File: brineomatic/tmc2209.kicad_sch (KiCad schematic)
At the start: 17 parts, among them J21 Conn_01x04, U9 TMC2209-LA

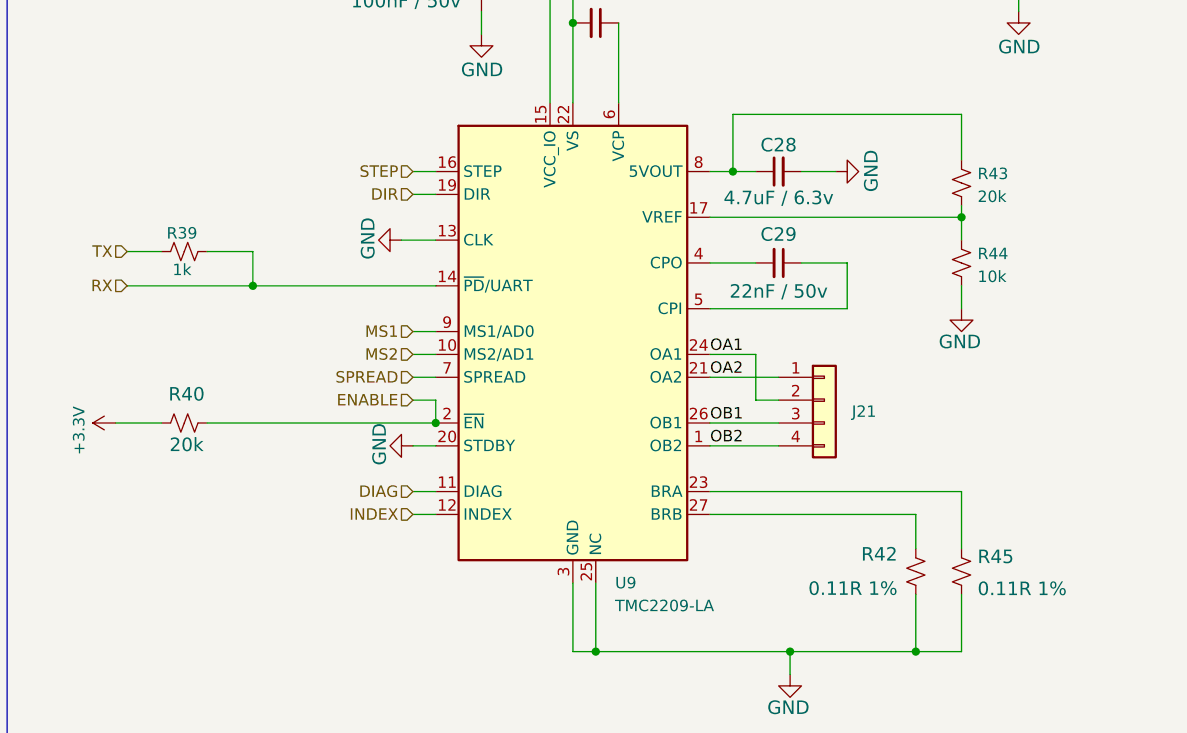
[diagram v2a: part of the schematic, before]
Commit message: switch to rt7272b for 24v -> 5v regulator
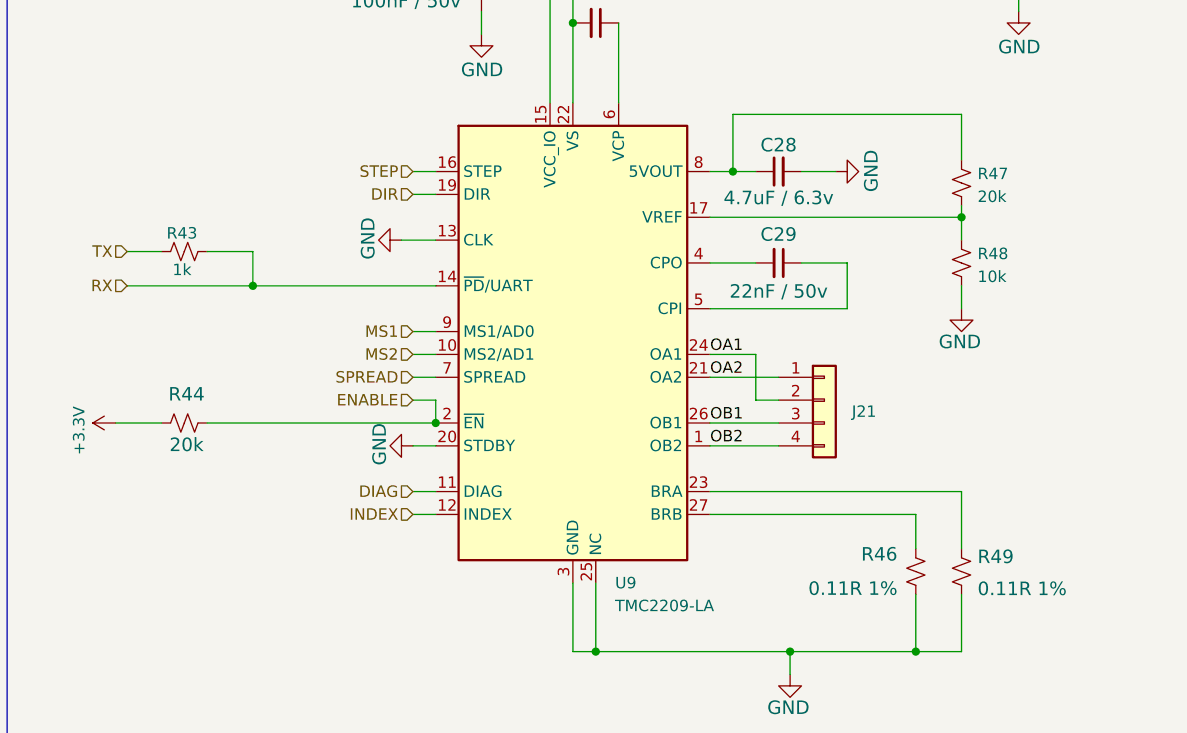
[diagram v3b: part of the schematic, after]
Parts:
- renumbered R39 to R43, R40 to R44, R42 to R46, R43 to R47, R44 to R48, R45 to R49
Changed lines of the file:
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@@
 		(on_board yes)
 		(dnp no)
-		(property "Reference" "R40"
+		(property "Reference" "R44"
 			(at 38.354 108.966 90)
 			(effects
@@
 			(project "brineomatic"
 				(path "/96477ae2-ef08-48f3-8dd4-fe4478541f68/0f01c39f-0c25-414e-9ed3-1ba09e2af0c5"
-					(reference "R40")
+					(reference "R44")
 					(unit 1)
 				)
@@
 		(on_board yes)
 		(dnp no)
-		(property "Reference" "R45"
+		(property "Reference" "R49"
 			(at 126.238 128.778 0)
 			(effects
@@
 			(project "brineomatic"
 				(path "/96477ae2-ef08-48f3-8dd4-fe4478541f68/0f01c39f-0c25-414e-9ed3-1ba09e2af0c5"
-					(reference "R45")
+					(reference "R49")
 					(unit 1)
 				)
@@
 		(on_board yes)
 		(dnp no)
-		(property "Reference" "R39"
+		(property "Reference" "R43"
 			(at 37.846 91.948 90)
 			(effects
@@
 			(project "brineomatic"
 				(path "/96477ae2-ef08-48f3-8dd4-fe4478541f68/0f01c39f-0c25-414e-9ed3-1ba09e2af0c5"
-					(reference "R39")
+					(reference "R43")
 					(unit 1)
 				)
@@
 		(on_board yes)
 		(dnp no)
-		(property "Reference" "#PWR063"
+		(property "Reference" "#PWR061"
 			(at 74.93 63.5 0)
 			(effects
@@
 			(project "brineomatic"
 				(path "/96477ae2-ef08-48f3-8dd4-fe4478541f68/0f01c39f-0c25-414e-9ed3-1ba09e2af0c5"
-					(reference "#PWR063")
+					(reference "#PWR061")
 					(unit 1)
 				)
@@
 		(on_board yes)
 		(dnp no)
-		(property "Reference" "R42"
+		(property "Reference" "R46"
 			(at 117.348 126.746 0)
 			(effects
@@
 			(project "brineomatic"
 				(path "/96477ae2-ef08-48f3-8dd4-fe4478541f68/0f01c39f-0c25-414e-9ed3-1ba09e2af0c5"
-					(reference "R42")
+					(reference "R46")
 					(unit 1)
 				)
@@
 		(on_board yes)
 		(dnp no)
-		(property "Reference" "#PWR062"
+		(property "Reference" "#PWR060"
 			(at 34.29 113.03 0)
 			(effects
@@
 			(project "brineomatic"
 				(path "/96477ae2-ef08-48f3-8dd4-fe4478541f68/0f01c39f-0c25-414e-9ed3-1ba09e2af0c5"
-					(reference "#PWR062")
+					(reference "#PWR060")
 					(unit 1)
 				)
@@
 		(on_board yes)
 		(dnp no)
-		(property "Reference" "R43"
+		(property "Reference" "R47"
 			(at 126.238 85.344 0)
 			(effects
@@
 			(project "brineomatic"
 				(path "/96477ae2-ef08-48f3-8dd4-fe4478541f68/0f01c39f-0c25-414e-9ed3-1ba09e2af0c5"
-					(reference "R43")
+					(reference "R47")
 					(unit 1)
 				)
@@
 		(dnp no)
 		(fields_autoplaced yes)
-		(property "Reference" "#PWR064"
+		(property "Reference" "#PWR062"
 			(at 81.28 52.07 0)
 			(effects
@@
 			(project ""
 				(path "/96477ae2-ef08-48f3-8dd4-fe4478541f68/0f01c39f-0c25-414e-9ed3-1ba09e2af0c5"
-					(reference "#PWR064")
+					(reference "#PWR062")
 					(unit 1)
 				)
@@
 		(on_board yes)
 		(dnp no)
-		(property "Reference" "R44"
+		(property "Reference" "R48"
 			(at 126.238 94.234 0)
 			(effects
@@
 			(project "brineomatic"
 				(path "/96477ae2-ef08-48f3-8dd4-fe4478541f68/0f01c39f-0c25-414e-9ed3-1ba09e2af0c5"
-					(reference "R44")
-					(unit 1)
-				)
+					(reference "R48")
+					(unit 1)
+				)

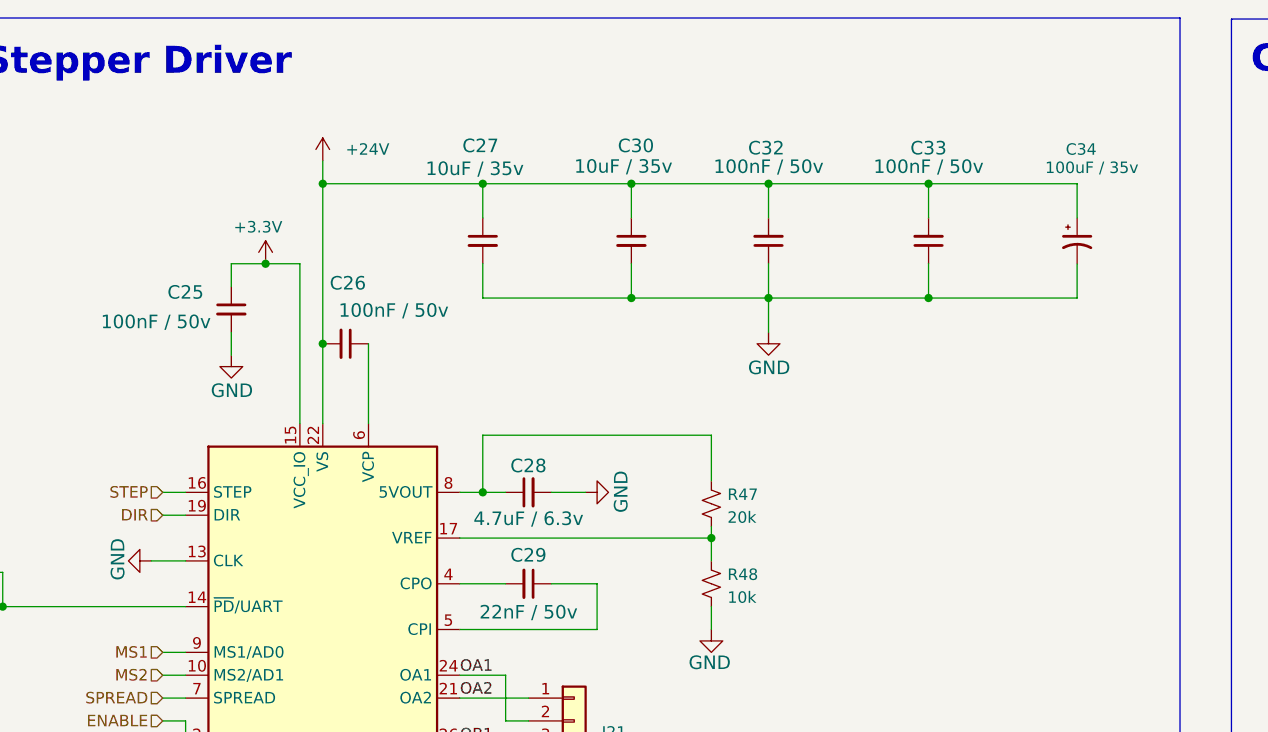
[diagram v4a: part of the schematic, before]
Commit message: added bulk cap to 5v rail and tidied silkscreen
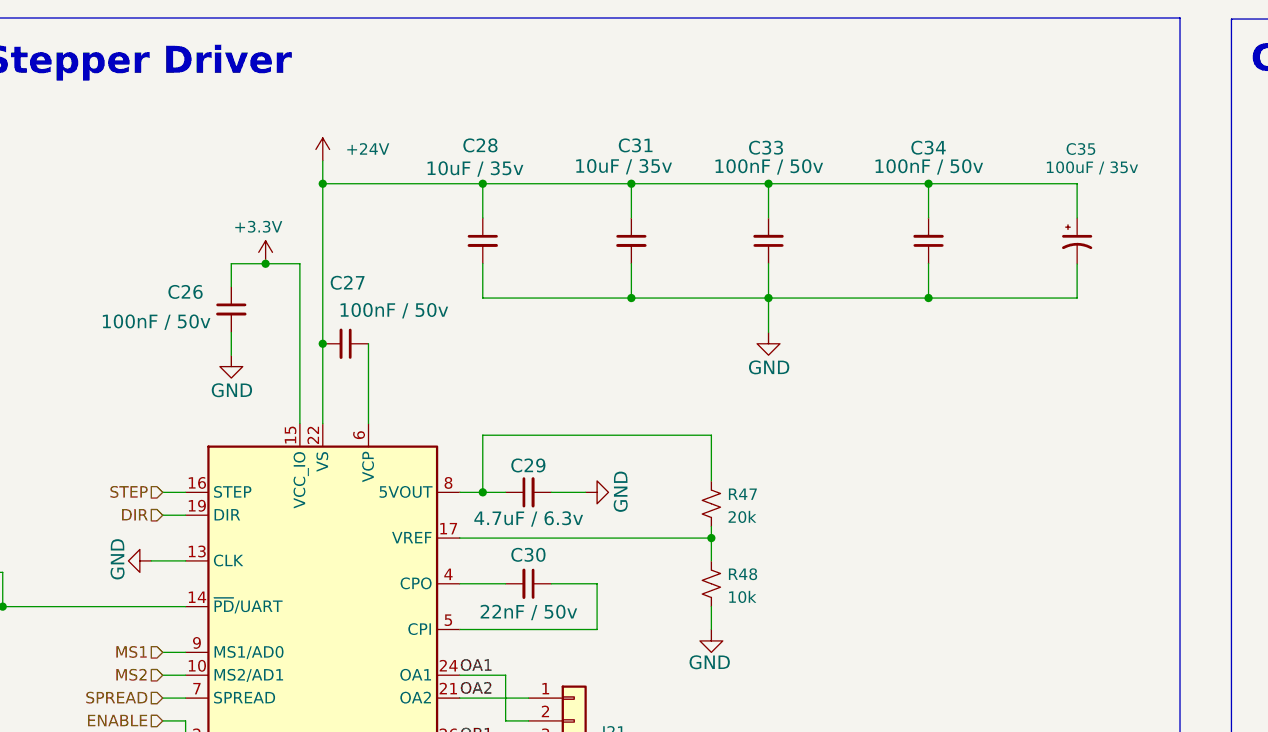
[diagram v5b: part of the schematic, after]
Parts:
- renumbered C25 to C26, C26 to C27, C27 to C28, C28 to C29, C29 to C30, C30 to C31, C32 to C33, C33 to C34, C34 to C35
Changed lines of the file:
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@@
 		(on_board yes)
 		(dnp no)
-		(property "Reference" "C30"
+		(property "Reference" "C31"
 			(at 118.11 45.72 0)
 			(effects
@@
 			(project "brineomatic"
 				(path "/96477ae2-ef08-48f3-8dd4-fe4478541f68/0f01c39f-0c25-414e-9ed3-1ba09e2af0c5"
-					(reference "C30")
+					(reference "C31")
 					(unit 1)
 				)
@@
 		(on_board yes)
 		(dnp no)
-		(property "Reference" "C33"
+		(property "Reference" "C34"
 			(at 148.59 45.974 0)
 			(effects
@@
 			(project "brineomatic"
 				(path "/96477ae2-ef08-48f3-8dd4-fe4478541f68/0f01c39f-0c25-414e-9ed3-1ba09e2af0c5"
-					(reference "C33")
+					(reference "C34")
 					(unit 1)
 				)
@@
 		(on_board yes)
 		(dnp no)
-		(property "Reference" "C26"
+		(property "Reference" "C27"
 			(at 84.074 62.738 90)
 			(effects
@@
 			(project "brineomatic"
 				(path "/96477ae2-ef08-48f3-8dd4-fe4478541f68/0f01c39f-0c25-414e-9ed3-1ba09e2af0c5"
-					(reference "C26")
+					(reference "C27")
 					(unit 1)
 				)
@@
 		(on_board yes)
 		(dnp no)
-		(property "Reference" "C34"
+		(property "Reference" "C35"
 			(at 163.83 46.99 0)
 			(effects
@@
 			(project ""
 				(path "/96477ae2-ef08-48f3-8dd4-fe4478541f68/0f01c39f-0c25-414e-9ed3-1ba09e2af0c5"
-					(reference "C34")
+					(reference "C35")
 					(unit 1)
 				)
@@
 		(on_board yes)
 		(dnp no)
-		(property "Reference" "C27"
+		(property "Reference" "C28"
 			(at 100.838 45.72 0)
 			(effects
@@
 			(project "brineomatic"
 				(path "/96477ae2-ef08-48f3-8dd4-fe4478541f68/0f01c39f-0c25-414e-9ed3-1ba09e2af0c5"
-					(reference "C27")
+					(reference "C28")
 					(unit 1)
 				)
@@
 		(on_board yes)
 		(dnp no)
-		(property "Reference" "C25"
+		(property "Reference" "C26"
 			(at 66.04 63.754 0)
 			(effects
@@
 			(project "brineomatic"
 				(path "/96477ae2-ef08-48f3-8dd4-fe4478541f68/0f01c39f-0c25-414e-9ed3-1ba09e2af0c5"
-					(reference "C25")
+					(reference "C26")
 					(unit 1)
 				)
@@
 		(on_board yes)
 		(dnp no)
-		(property "Reference" "C29"
+		(property "Reference" "C30"
 			(at 104.14 92.964 90)
 			(effects
@@
 			(project "brineomatic"
 				(path "/96477ae2-ef08-48f3-8dd4-fe4478541f68/0f01c39f-0c25-414e-9ed3-1ba09e2af0c5"
-					(reference "C29")
+					(reference "C30")
 					(unit 1)
 				)
@@
 		(on_board yes)
 		(dnp no)
-		(property "Reference" "C28"
+		(property "Reference" "C29"
 			(at 104.14 81.28 90)
 			(effects
@@
 			(project "brineomatic"
 				(path "/96477ae2-ef08-48f3-8dd4-fe4478541f68/0f01c39f-0c25-414e-9ed3-1ba09e2af0c5"
-					(reference "C28")
+					(reference "C29")
 					(unit 1)
 				)
@@
 		(on_board yes)
 		(dnp no)
-		(property "Reference" "C32"
+		(property "Reference" "C33"
 			(at 130.556 45.974 0)
 			(effects
@@
 			(project "brineomatic"
 				(path "/96477ae2-ef08-48f3-8dd4-fe4478541f68/0f01c39f-0c25-414e-9ed3-1ba09e2af0c5"
-					(reference "C32")
-					(unit 1)
-				)
+					(reference "C33")
+					(unit 1)
+				)

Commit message: tested and update bom + placement
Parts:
- C26, C27: value 100nF / 50v -> 100nF; LCSC (none) -> C14663
- C29: value 4.7uF / 6.3v -> 4.7uF; LCSC (none) -> C19666
- C30: LCSC C21122 -> (none)
- C33, C34: value 100nF / 50v -> 100nF; footprint Capacitor_SMD:C_0402_1005Metric -> Capacitor_SMD:C_0603_1608Metric; LCSC (none) -> C14663
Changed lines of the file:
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@@
 			)
 		)
-		(property "Value" "100nF / 50v"
+		(property "Value" "100nF"
 			(at 148.59 49.784 0)
 			(effects
@@
 			)
 		)
-		(property "Footprint" "Capacitor_SMD:C_0402_1005Metric"
+		(property "Footprint" "Capacitor_SMD:C_0603_1608Metric"
 			(at 148.59 57.15 0)
 			(effects
@@
 			)
 		)
-		(property "LCSC" ""
+		(property "LCSC" "C14663"
 			(at 148.59 57.15 0)
 			(effects
@@
 			)
 		)
-		(property "Value" "100nF / 50v"
+		(property "Value" "100nF"
 			(at 89.154 64.008 90)
 			(effects
@@
 			)
 		)
-		(property "LCSC" ""
+		(property "LCSC" "C14663"
 			(at 83.82 68.58 90)
 			(effects
@@
 			)
 		)
-		(property "Value" "100nF / 50v"
+		(property "Value" "100nF"
 			(at 62.738 65.278 0)
 			(effects
@@
 			)
 		)
-		(property "LCSC" ""
+		(property "LCSC" "C14663"
 			(at 71.12 64.77 0)
 			(effects
@@
 			)
 		)
-		(property "LCSC" "C21122"
+		(property "LCSC" ""
 			(at 104.14 95.25 90)
 			(effects
@@
 			)
 		)
-		(property "Value" "4.7uF / 6.3v"
+		(property "Value" "4.7uF"
 			(at 104.14 88.9 90)
 			(effects
@@
 			)
 		)
-		(property "LCSC" ""
+		(property "LCSC" "C19666"
 			(at 104.14 85.09 90)
 			(effects
@@
 			)
 		)
-		(property "Value" "100nF / 50v"
+		(property "Value" "100nF"
 			(at 130.81 49.784 0)
 			(effects
@@
 			)
 		)
-		(property "Footprint" "Capacitor_SMD:C_0402_1005Metric"
+		(property "Footprint" "Capacitor_SMD:C_0603_1608Metric"
 			(at 130.81 57.15 0)
 			(effects
@@
 			)
 		)
-		(property "LCSC" ""
+		(property "LCSC" "C14663"
 			(at 130.81 57.15 0)
 			(effects

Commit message: updated resistor p/ns in bom
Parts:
- R43: LCSC (none) -> C21190
- R44, R47: LCSC (none) -> C4184
- R48: LCSC (none) -> C25804
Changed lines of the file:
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@@
+			)
+		)
+		(property "LCSC" " C4184"
+			(at 38.1 113.03 90)
+			(effects
+				(font
+					(size 1.27 1.27)
+				)
+				(hide yes)
 			)
 		)
@@
 		(property "Description" "Resistor, small US symbol"
 			(at 38.1 93.98 0)
+			(effects
+				(font
+					(size 1.27 1.27)
+				)
+				(hide yes)
+			)
+		)
+		(property "LCSC" " C21190"
+			(at 38.1 93.98 90)
 			(effects
 				(font
@@
 			)
 		)
+		(property "LCSC" " C4184"
+			(at 124.46 86.36 0)
+			(effects
+				(font
+					(size 1.27 1.27)
+				)
+				(hide yes)
+			)
+		)
 		(pin "1"
 		)
@@
 			(at 124.46 95.25 0)
 			(effects
+				(font
+					(size 1.27 1.27)
+				)
+				(hide yes)
+			)
+		)
+		(property "LCSC" "C25804"
+			(at 124.46 95.25 0)
+			(effects
